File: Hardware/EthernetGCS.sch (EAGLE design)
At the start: 65 parts, among them IC3 24AA00OT, IC4 PIC24FJ64GA002_QFN, J2 HR911105A, Q2 25Mhz, U1 MIC5219-3.3V, U3 MIC5219-3.3V, U4 ENC28J60-QFN, U5 MIC5219-3.3V, U7 FT232RL-BASICSSOP, X2 USB-A-H

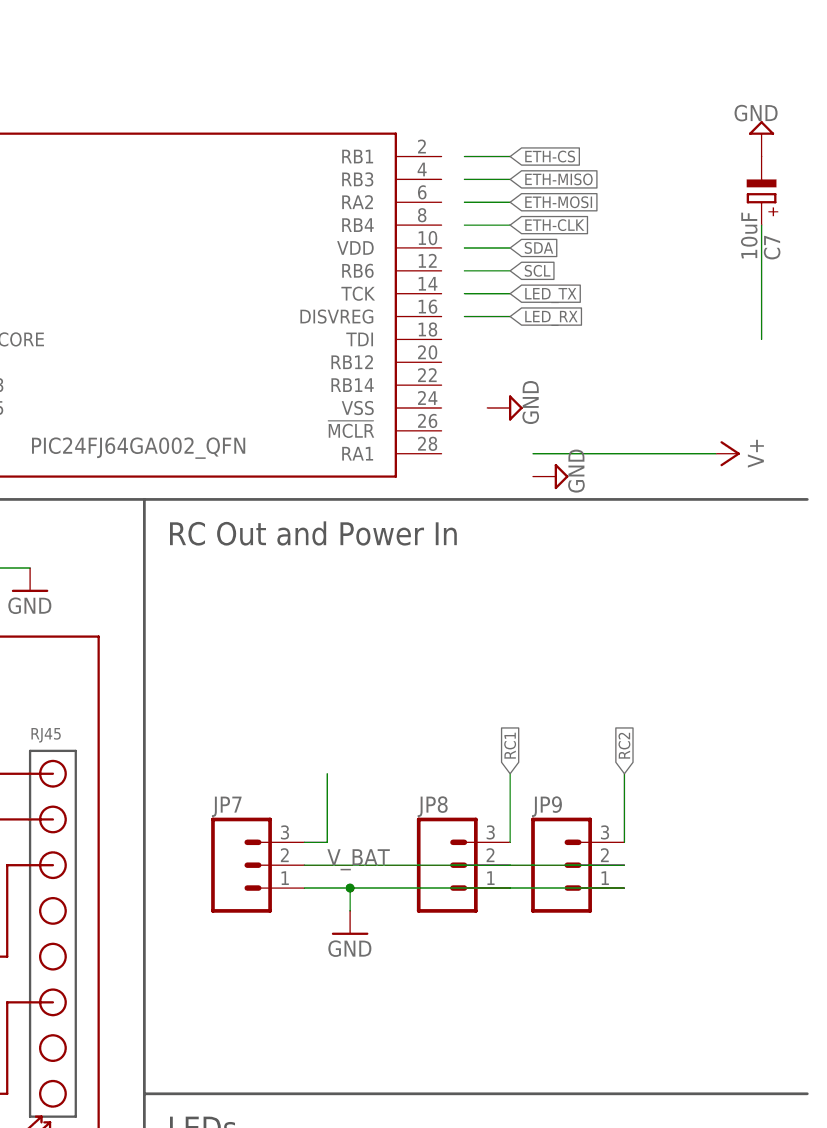
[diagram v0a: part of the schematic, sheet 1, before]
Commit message: Adding a sense line for the batterie
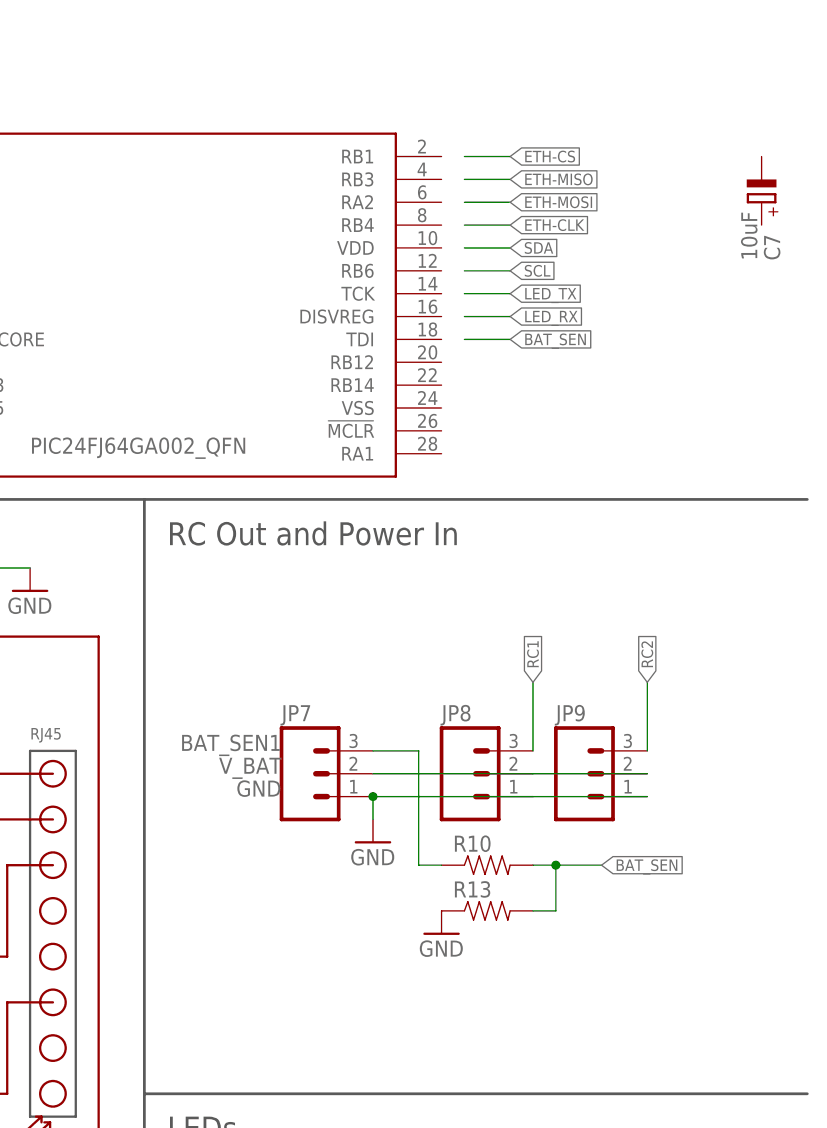
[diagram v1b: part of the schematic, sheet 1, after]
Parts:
- added R10, R13: (no value), SparkFun:RESISTOR0402-RES
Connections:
- removed net BAT_MON: JP7.3
- removed net N$16: C7.+
- new net BAT_SEN: R10.2, R13.2
- new net BAT_SEN1: JP7.3, R10.1
- net GND: now also R13.1; no longer C7.-
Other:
- moved on the sheet: JP7, JP8, JP9
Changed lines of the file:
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@@
 <part name="V2" library="supply2" deviceset="GND" device=""/>
 <part name="Q2" library="crystal" deviceset="CRYSTAL" device="CTS406" value="25Mhz"/>
-<part name="V3" library="supply2" deviceset="GND" device=""/>
 <part name="C7" library="rcl" deviceset="CPOL-EU" device="SMCA" value="10uF"/>
-<part name="V4" library="supply2" deviceset="GND" device=""/>
-<part name="P+3" library="supply2" deviceset="V+" device=""/>
-<part name="V5" library="supply2" deviceset="GND" device=""/>
 <part name="P+5" library="supply2" deviceset="V+" device=""/>
 <part name="P+6" library="supply2" deviceset="V+" device=""/>
@@
 <part name="L1" library="pel_dipol_comp" deviceset="INDUCTOR" device="-0402" value="BLM15HD102SN1"/>
 <part name="GND28" library="supply1" deviceset="GND" device=""/>
+<part name="R10" library="SparkFun" deviceset="RESISTOR" device="0402-RES"/>
+<part name="R13" library="SparkFun" deviceset="RESISTOR" device="0402-RES"/>
+<part name="GND29" library="supply1" deviceset="GND" device=""/>
 </parts>
 <sheets>
@@
 <attribute name="VALUE" x="78.74" y="81.788" size="1.778" layer="96"/>
 </instance>
-<instance part="V3" gate="GND" x="215.9" y="142.24" rot="R90"/>
 <instance part="C7" gate="G$1" x="243.84" y="165.1" smashed="yes" rot="R180">
 <attribute name="NAME" x="245.8974" y="158.623" size="1.778" layer="95" rot="R90"/>
 <attribute name="VALUE" x="243.3574" y="158.623" size="1.778" layer="96" rot="R90"/>
 </instance>
-<instance part="V4" gate="GND" x="243.84" y="172.72" rot="R180"/>
-<instance part="P+3" gate="1" x="241.3" y="137.16" smashed="yes" rot="R270">
-<attribute name="VALUE" x="242.316" y="138.938" size="1.778" layer="96" rot="R270"/>
-</instance>
-<instance part="V5" gate="GND" x="220.98" y="134.62" rot="R90"/>
 <instance part="P+5" gate="1" x="45.72" y="99.06" smashed="yes">
 <attribute name="VALUE" x="50.038" y="98.806" size="1.778" layer="96"/>
@@
 <instance part="U$2" gate="G$1" x="76.2" y="170.18"/>
 <instance part="P+4" gate="G$1" x="129.54" y="170.18"/>
-<instance part="JP7" gate="G$1" x="185.42" y="91.44"/>
-<instance part="JP8" gate="G$1" x="208.28" y="91.44"/>
-<instance part="JP9" gate="G$1" x="220.98" y="91.44"/>
+<instance part="JP7" gate="G$1" x="193.04" y="101.6"/>
+<instance part="JP8" gate="G$1" x="210.82" y="101.6"/>
+<instance part="JP9" gate="G$1" x="223.52" y="101.6"/>
 <instance part="L1" gate="G$1" x="111.76" y="93.98" smashed="yes" rot="R180">
 <attribute name="NAME" x="111.2774" y="88.392" size="1.778" layer="95" rot="R90"/>
 </instance>
-<instance part="GND28" gate="1" x="198.12" y="83.82"/>
+<instance part="GND28" gate="1" x="200.66" y="93.98"/>
+<instance part="R10" gate="G$1" x="213.36" y="91.44" smashed="yes">
+<attribute name="NAME" x="209.55" y="92.9386" size="1.778" layer="95"/>
+<attribute name="VALUE" x="216.408" y="89.154" size="1.778" layer="96"/>
+</instance>
+<instance part="R13" gate="G$1" x="213.36" y="86.36" smashed="yes">
+<attribute name="NAME" x="209.55" y="87.8586" size="1.778" layer="95"/>
+<attribute name="VALUE" x="216.408" y="84.074" size="1.778" layer="96"/>
+</instance>
+<instance part="GND29" gate="1" x="208.28" y="83.82"/>
 </instances>
 <busses>
@@
 </segment>
 <segment>
-<pinref part="C7" gate="G$1" pin="-"/>
-<pinref part="V4" gate="GND" pin="GND"/>
-</segment>
-<segment>
 <wire x1="30.48" y1="48.26" x2="40.64" y2="48.26" width="0.1524" layer="91"/>
 <wire x1="40.64" y1="48.26" x2="45.72" y2="48.26" width="0.1524" layer="91"/>
@@
 <pinref part="JP7" gate="G$1" pin="1"/>
 <pinref part="JP8" gate="G$1" pin="1"/>
-<wire x1="193.04" y1="88.9" x2="198.12" y2="88.9" width="0.1524" layer="91"/>
 <pinref part="JP9" gate="G$1" pin="1"/>
-<wire x1="198.12" y1="88.9" x2="215.9" y2="88.9" width="0.1524" layer="91"/>
-<wire x1="215.9" y1="88.9" x2="228.6" y2="88.9" width="0.1524" layer="91"/>
+<wire x1="200.66" y1="99.06" x2="218.44" y2="99.06" width="0.1524" layer="91"/>
+<wire x1="218.44" y1="99.06" x2="231.14" y2="99.06" width="0.1524" layer="91"/>
 <pinref part="GND28" gate="1" pin="GND"/>
-<wire x1="198.12" y1="86.36" x2="198.12" y2="88.9" width="0.1524" layer="91"/>
-<junction x="198.12" y="88.9"/>
+<wire x1="200.66" y1="96.52" x2="200.66" y2="99.06" width="0.1524" layer="91"/>
+<junction x="200.66" y="99.06"/>
+<label x="190.5" y="99.06" size="1.778" layer="95" rot="MR0"/>
+</segment>
+<segment>
+<pinref part="R13" gate="G$1" pin="1"/>
+<pinref part="GND29" gate="1" pin="GND"/>
 </segment>
 </net>
@@
 </net>
 <net name="V+" class="0">
-<segment>
-<wire x1="238.76" y1="137.16" x2="218.44" y2="137.16" width="0.1524" layer="91"/>
-<pinref part="P+3" gate="1" pin="V+"/>
-</segment>
 <segment>
 <wire x1="38.1" y1="114.3" x2="40.64" y2="114.3" width="0.1524" layer="91"/>
@@
 <junction x="83.82" y="78.74"/>
 <wire x1="83.82" y1="78.74" x2="81.28" y2="78.74" width="0.1524" layer="91"/>
-</segment>
-</net>
-<net name="N$16" class="0">
-<segment>
-<wire x1="243.84" y1="162.56" x2="243.84" y2="149.86" width="0.1524" layer="91"/>
-<pinref part="C7" gate="G$1" pin="+"/>
 </segment>
 </net>
@@
 <pinref part="JP7" gate="G$1" pin="2"/>
 <pinref part="JP8" gate="G$1" pin="2"/>
-<wire x1="193.04" y1="91.44" x2="215.9" y2="91.44" width="0.1524" layer="91"/>
+<wire x1="200.66" y1="101.6" x2="218.44" y2="101.6" width="0.1524" layer="91"/>
 <pinref part="JP9" gate="G$1" pin="2"/>
-<wire x1="215.9" y1="91.44" x2="228.6" y2="91.44" width="0.1524" layer="91"/>
-<label x="195.58" y="91.44" size="1.778" layer="95"/>
-</segment>
-</net>
-<net name="BAT_MON" class="0">
+<wire x1="218.44" y1="101.6" x2="231.14" y2="101.6" width="0.1524" layer="91"/>
+<label x="190.5" y="101.6" size="1.778" layer="95" rot="MR0"/>
+</segment>
+</net>
+<net name="BAT_SEN1" class="0">
 <segment>
 <pinref part="JP7" gate="G$1" pin="3"/>
-<wire x1="193.04" y1="93.98" x2="195.58" y2="93.98" width="0.1524" layer="91"/>
-<wire x1="195.58" y1="93.98" x2="195.58" y2="101.6" width="0.1524" layer="91"/>
+<wire x1="200.66" y1="104.14" x2="205.74" y2="104.14" width="0.1524" layer="91"/>
+<wire x1="205.74" y1="104.14" x2="205.74" y2="91.44" width="0.1524" layer="91"/>
+<pinref part="R10" gate="G$1" pin="1"/>
+<wire x1="208.28" y1="91.44" x2="205.74" y2="91.44" width="0.1524" layer="91"/>
+<label x="190.5" y="104.14" size="1.778" layer="95" rot="MR0"/>
 </segment>
 </net>
@@
 <segment>
 <pinref part="JP8" gate="G$1" pin="3"/>
-<wire x1="215.9" y1="93.98" x2="215.9" y2="101.6" width="0.1524" layer="91"/>
-<label x="215.9" y="101.6" size="1.27" layer="95" rot="R90" xref="yes"/>
+<wire x1="218.44" y1="104.14" x2="218.44" y2="111.76" width="0.1524" layer="91"/>
+<label x="218.44" y="111.76" size="1.27" layer="95" rot="R90" xref="yes"/>
 </segment>
 </net>
@@
 <segment>
 <pinref part="JP9" gate="G$1" pin="3"/>
-<wire x1="228.6" y1="93.98" x2="228.6" y2="101.6" width="0.1524" layer="91"/>
-<label x="228.6" y="101.6" size="1.27" layer="95" rot="R90" xref="yes"/>
-</segment>
-</net>
+<wire x1="231.14" y1="104.14" x2="231.14" y2="111.76" width="0.1524" layer="91"/>
+<label x="231.14" y="111.76" size="1.27" layer="95" rot="R90" xref="yes"/>
+</segment>
+</net>
+<net name="BAT_SEN" class="0">
+<segment>
+<pinref part="R13" gate="G$1" pin="2"/>
+<wire x1="218.44" y1="86.36" x2="220.98" y2="86.36" width="0.1524" layer="91"/>
+<wire x1="220.98" y1="86.36" x2="220.98" y2="91.44" width="0.1524" layer="91"/>
+<pinref part="R10" gate="G$1" pin="2"/>
+<wire x1="220.98" y1="91.44" x2="218.44" y2="91.44" width="0.1524" layer="91"/>
+<wire x1="220.98" y1="91.44" x2="226.06" y2="91.44" width="0.1524" layer="91"/>
+<junction x="220.98" y="91.44"/>
+<label x="226.06" y="91.44" size="1.27" layer="95" xref="yes"/>
+<wire x1="210.82" y1="149.86" x2="215.9" y2="149.86" width="0.1524" layer="91"/>
+<label x="215.9" y="149.86" size="1.27" layer="95" xref="yes"/>
+</segment>
+</net>

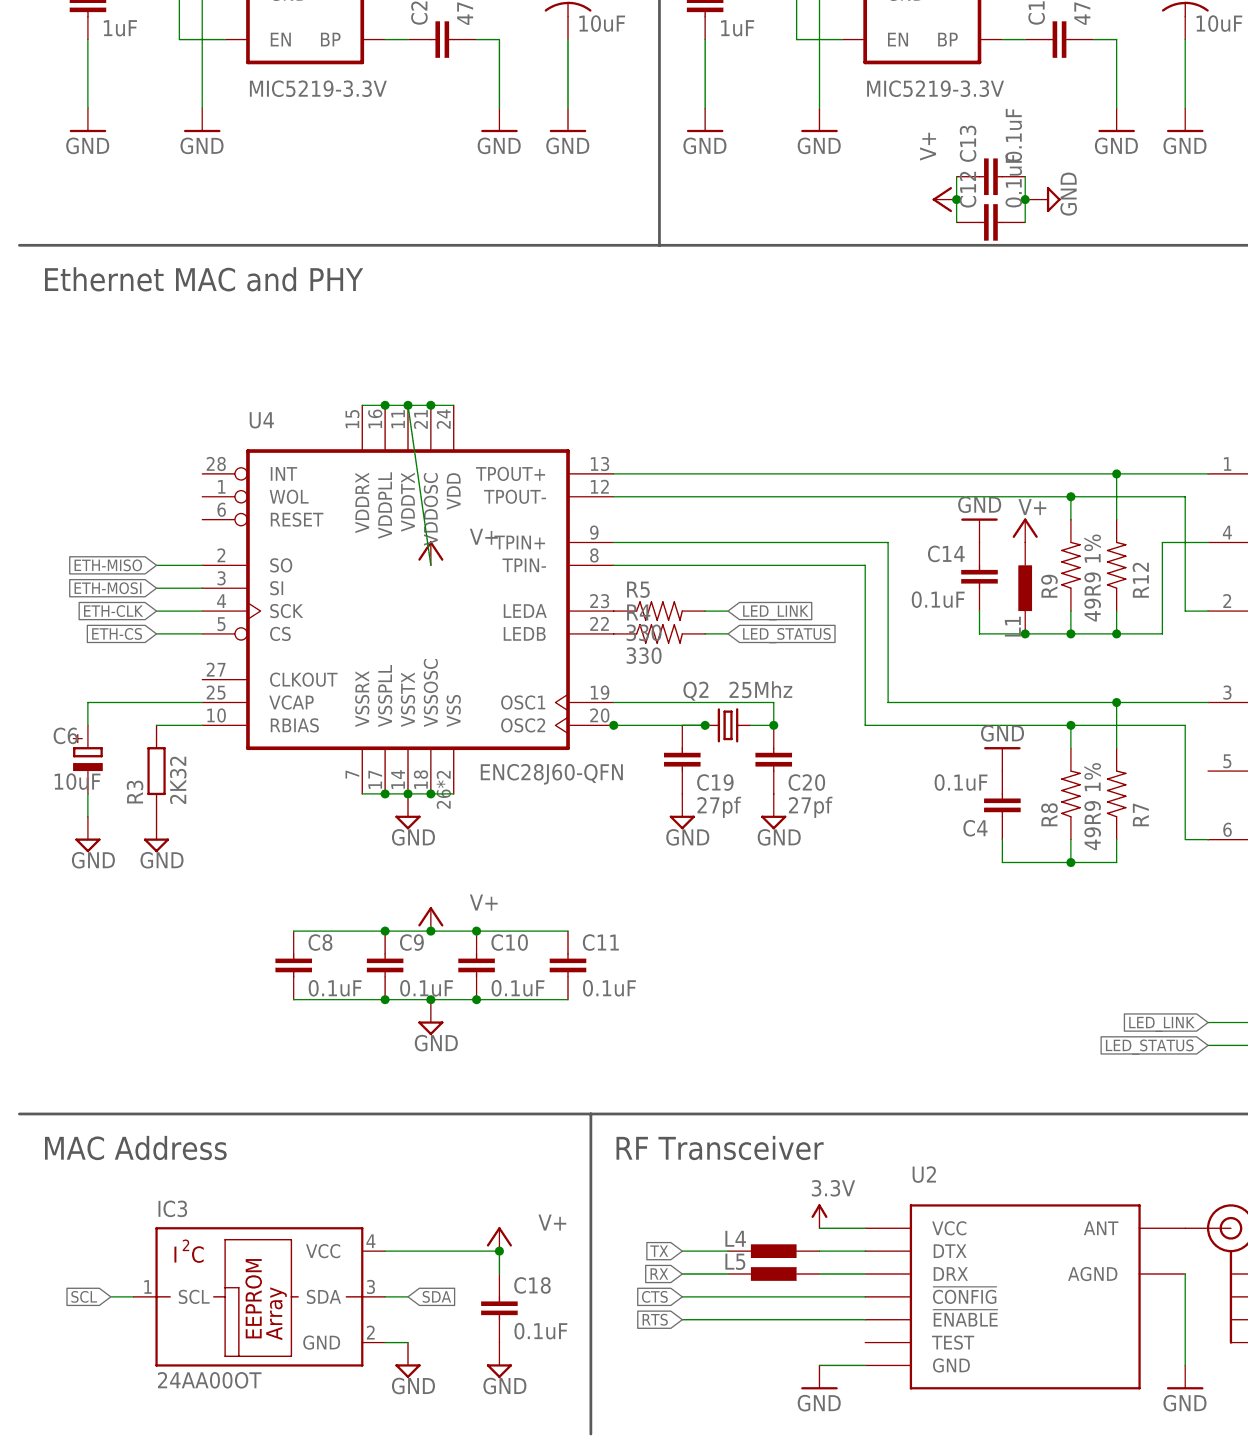
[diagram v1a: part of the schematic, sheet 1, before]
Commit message: Fix the problem of multiple ground symbols
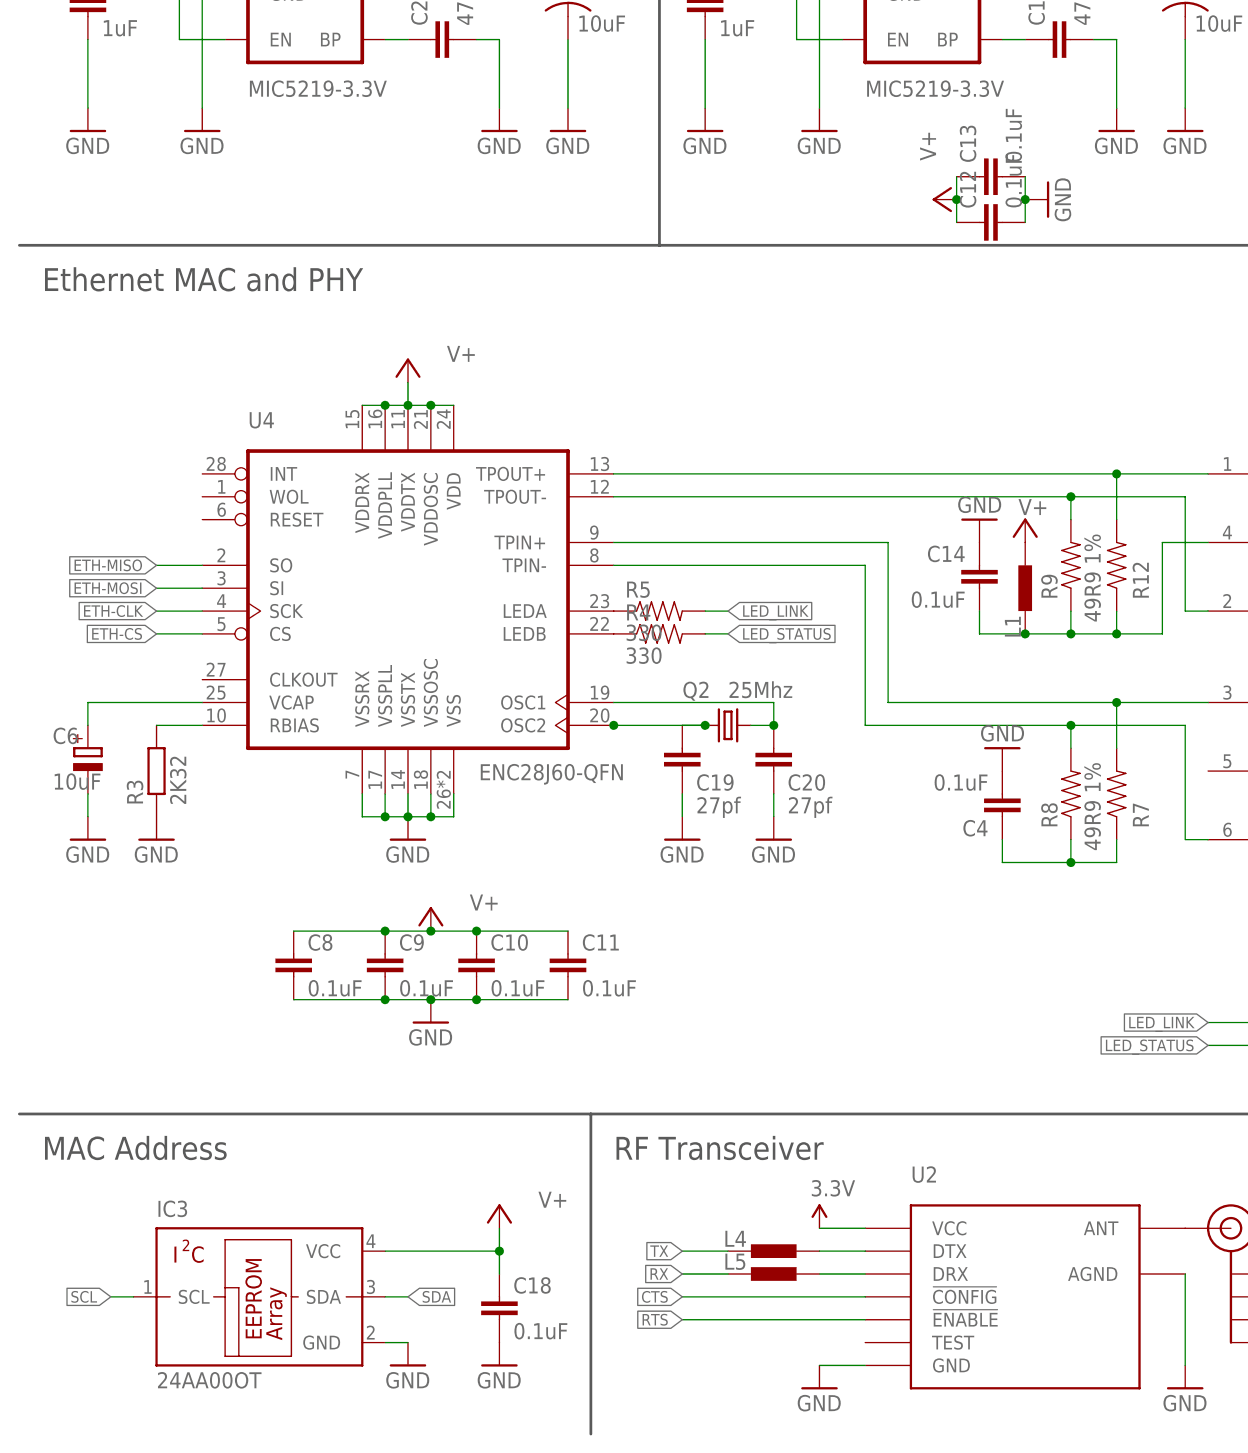
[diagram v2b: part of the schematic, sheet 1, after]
